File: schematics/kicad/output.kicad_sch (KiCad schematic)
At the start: 33 parts, among them J7 DE15_Socket_HighDensity, K1300 10uF, U1300 HM53461, U1301 HM53461, U1302 HM53461, U1303 HM53461, U1304 HM53461, U1305 HM53461, U1306 HM53461, U1307 HM53461, U1310 BT458, U1311 92.9405Mhz, U1312 10H101, U1313 10H131, U1314 10H350, U1315 LM385BZ-1.2, U1318 74F08

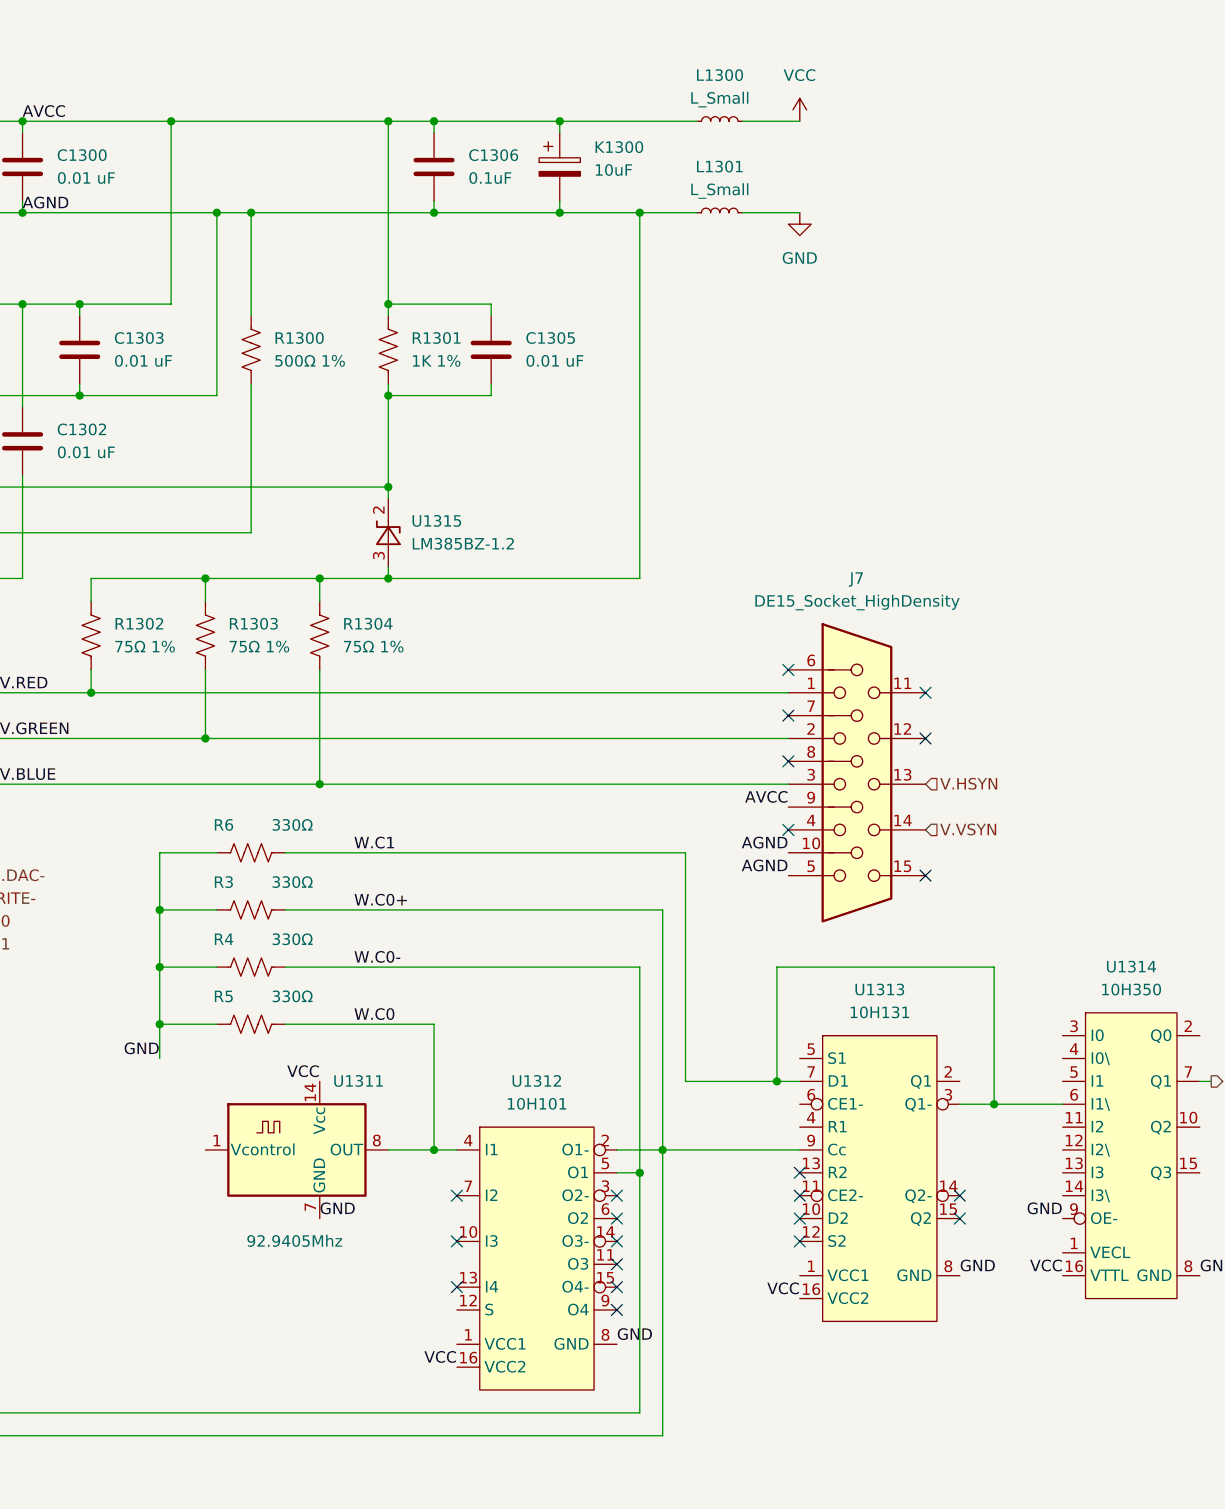
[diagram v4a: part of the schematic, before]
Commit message: Fix layout of the memory chips based on the board Fix the orientation of the P4 connector Connect CS.DAC- based on the board Change the orientation of the ECL resistors to route better Fix the copper islands to match the board, only DAC is on analog island, ECL and crystal are separate. Fix ECL VCC to VCC Confirm VEE not used Add PALs - U1000 missing
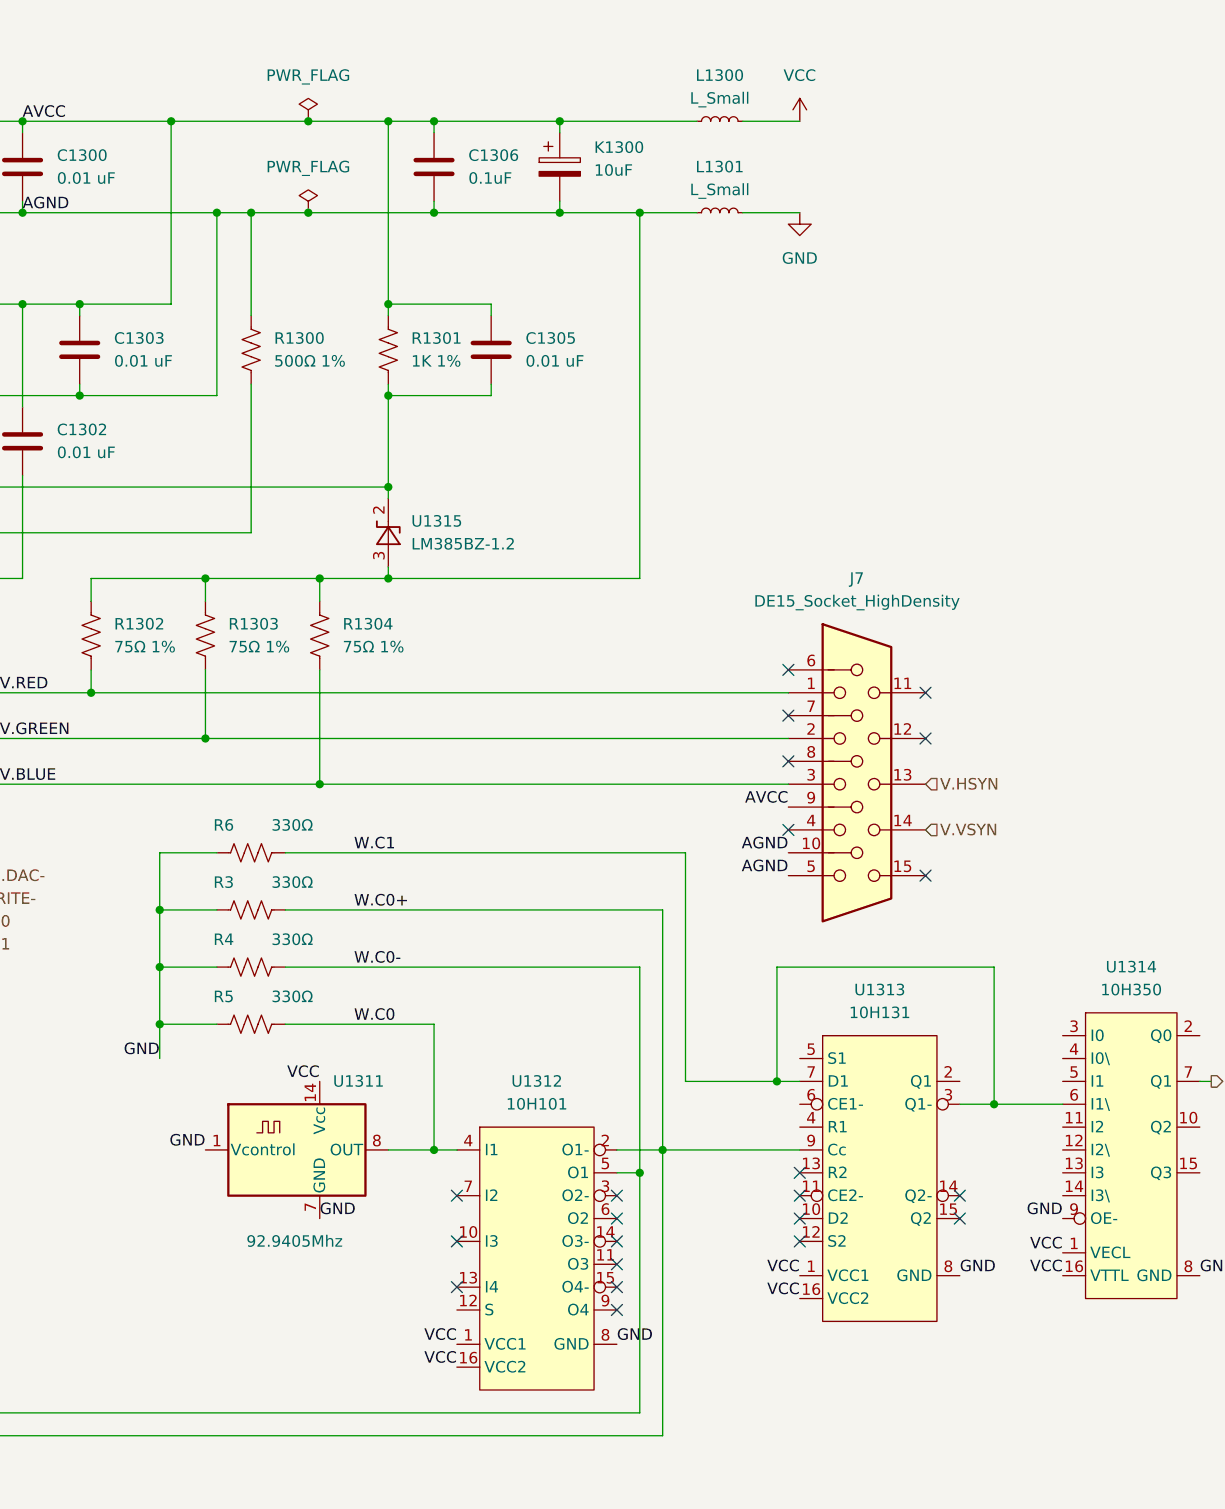
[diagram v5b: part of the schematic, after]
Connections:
- net GND: now also U1311.1 (Vcontrol)
- net VCC: now also U1312.1 (VCC1), U1313.1 (VCC1), U1314.1 (VECL)
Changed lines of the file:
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@@
 	)
 	(junction
+		(at 226.06 24.13)
+		(diameter 0)
+		(color 0 0 0 0)
+	)
+	(junction
 		(at 278.13 130.81)
 		(diameter 0)
@@
 	)
 	(junction
+		(at 226.06 34.29)
+		(diameter 0)
+		(color 0 0 0 0)
+	)
+	(junction
 		(at 55.88 104.14)
 		(diameter 0)
@@
 	(wire
 		(pts
-			(xy 210.82 24.13) (xy 234.95 24.13)
+			(xy 210.82 24.13) (xy 226.06 24.13)
 		)
 		(stroke
@@
 	(wire
 		(pts
+			(xy 226.06 34.29) (xy 240.03 34.29)
+		)
+		(stroke
+			(width 0)
+			(type default)
+		)
+	)
+	(wire
+		(pts
 			(xy 63.5 135.89) (xy 83.82 135.89)
 		)
@@
 	(wire
 		(pts
+			(xy 226.06 24.13) (xy 234.95 24.13)
+		)
+		(stroke
+			(width 0)
+			(type default)
+		)
+	)
+	(wire
+		(pts
 			(xy 214.63 74.93) (xy 227.33 74.93)
 		)
@@
 	(wire
 		(pts
-			(xy 219.71 34.29) (xy 240.03 34.29)
+			(xy 219.71 34.29) (xy 226.06 34.29)
 		)
 		(stroke
@@
 		)
 	)
+	(label "GND"
+		(at 214.63 138.43 180)
+		(effects
+			(font
+				(size 1.27 1.27)
+			)
+			(justify right bottom)
+		)
+	)
 	(label "AGND"
 		(at 279.4 105.41 180)
@@
 		)
 	)
+	(label "VCC"
+		(at 242.57 160.02 180)
+		(effects
+			(font
+				(size 1.27 1.27)
+			)
+			(justify right bottom)
+		)
+	)
 	(label "V.D.D9"
 		(at 130.81 121.92 180)
@@
 		)
 	)
+	(label "VCC"
+		(at 280.67 152.4 180)
+		(effects
+			(font
+				(size 1.27 1.27)
+			)
+			(justify right bottom)
+		)
+	)
 	(label "W.RE-51"
 		(at 76.2 139.7 0)
@@
 		)
 	)
+	(label "VCC"
+		(at 309.88 149.86 180)
+		(effects
+			(font
+				(size 1.27 1.27)
+			)
+			(justify right bottom)
+		)
+	)
 	(label "V.D.D3"
 		(at 163.83 105.41 180)
@@
 	)
 	(symbol
+		(lib_id "power:PWR_FLAG")
+		(at 226.06 34.29 0)
+		(unit 1)
+		(exclude_from_sim no)
+		(in_bom yes)
+		(on_board yes)
+		(dnp no)
+		(fields_autoplaced yes)
+		(property "Reference" "#FLG04"
+			(at 226.06 32.385 0)
+			(effects
+				(font
+					(size 1.27 1.27)
+				)
+				(hide yes)
+			)
+		)
+		(property "Value" "PWR_FLAG"
+			(at 226.06 29.21 0)
+			(effects
+				(font
+					(size 1.27 1.27)
+				)
+			)
+		)
+		(property "Footprint" ""
+			(at 226.06 34.29 0)
+			(effects
+				(font
+					(size 1.27 1.27)
+				)
+				(hide yes)
+			)
+		)
+		(property "Datasheet" "~"
+			(at 226.06 34.29 0)
+			(effects
+				(font
+					(size 1.27 1.27)
+				)
+				(hide yes)
+			)
+		)
+		(property "Description" "Special symbol for telling ERC where power comes from"
+			(at 226.06 34.29 0)
+			(effects
+				(font
+					(size 1.27 1.27)
+				)
+				(hide yes)
+			)
+		)
+		(pin "1"
+		)
+		(instances
+			(project "cg4"
+				(path "/7c2b6a13-c303-4adb-8eed-6e6a9ac5307e/29ede95e-baf3-44af-bd6e-b3be323fd399"
+					(reference "#FLG04")
+					(unit 1)
+				)
+			)
+		)
+	)
+	(symbol
 		(lib_id "power:GND")
 		(at 280.67 34.29 0)
@@
 					(unit 1)
 				)
+			)
+		)
+	)
+	(symbol
+		(lib_id "power:PWR_FLAG")
+		(at 226.06 24.13 0)
+		(unit 1)
+		(exclude_from_sim no)
+		(in_bom yes)
+		(on_board yes)
+		(dnp no)
+		(fields_autoplaced yes)
+		(property "Reference" "#FLG03"
+			(at 226.06 22.225 0)
+			(effects
+				(font
+					(size 1.27 1.27)
+				)
+				(hide yes)
+			)
+		)
+		(property "Value" "PWR_FLAG"
+			(at 226.06 19.05 0)
+			(effects
+				(font
+					(size 1.27 1.27)
+				)
+			)
+		)
+		(property "Footprint" ""
+			(at 226.06 24.13 0)
+			(effects
+				(font
+					(size 1.27 1.27)
+				)
+				(hide yes)
+			)
+		)
+		(property "Datasheet" "~"
+			(at 226.06 24.13 0)
+			(effects
+				(font
+					(size 1.27 1.27)
+				)
+				(hide yes)
+			)
+		)
+		(property "Description" "Special symbol for telling ERC where power comes from"
+			(at 226.06 24.13 0)
+			(effects
+				(font
+					(size 1.27 1.27)
+				)
+				(hide yes)
+			)
+		)
+		(pin "1"
+		)
+		(instances
+			(project "cg4"
+				(path "/7c2b6a13-c303-4adb-8eed-6e6a9ac5307e/29ede95e-baf3-44af-bd6e-b3be323fd399"
+					(reference "#FLG03")
+					(unit 1)
+				)

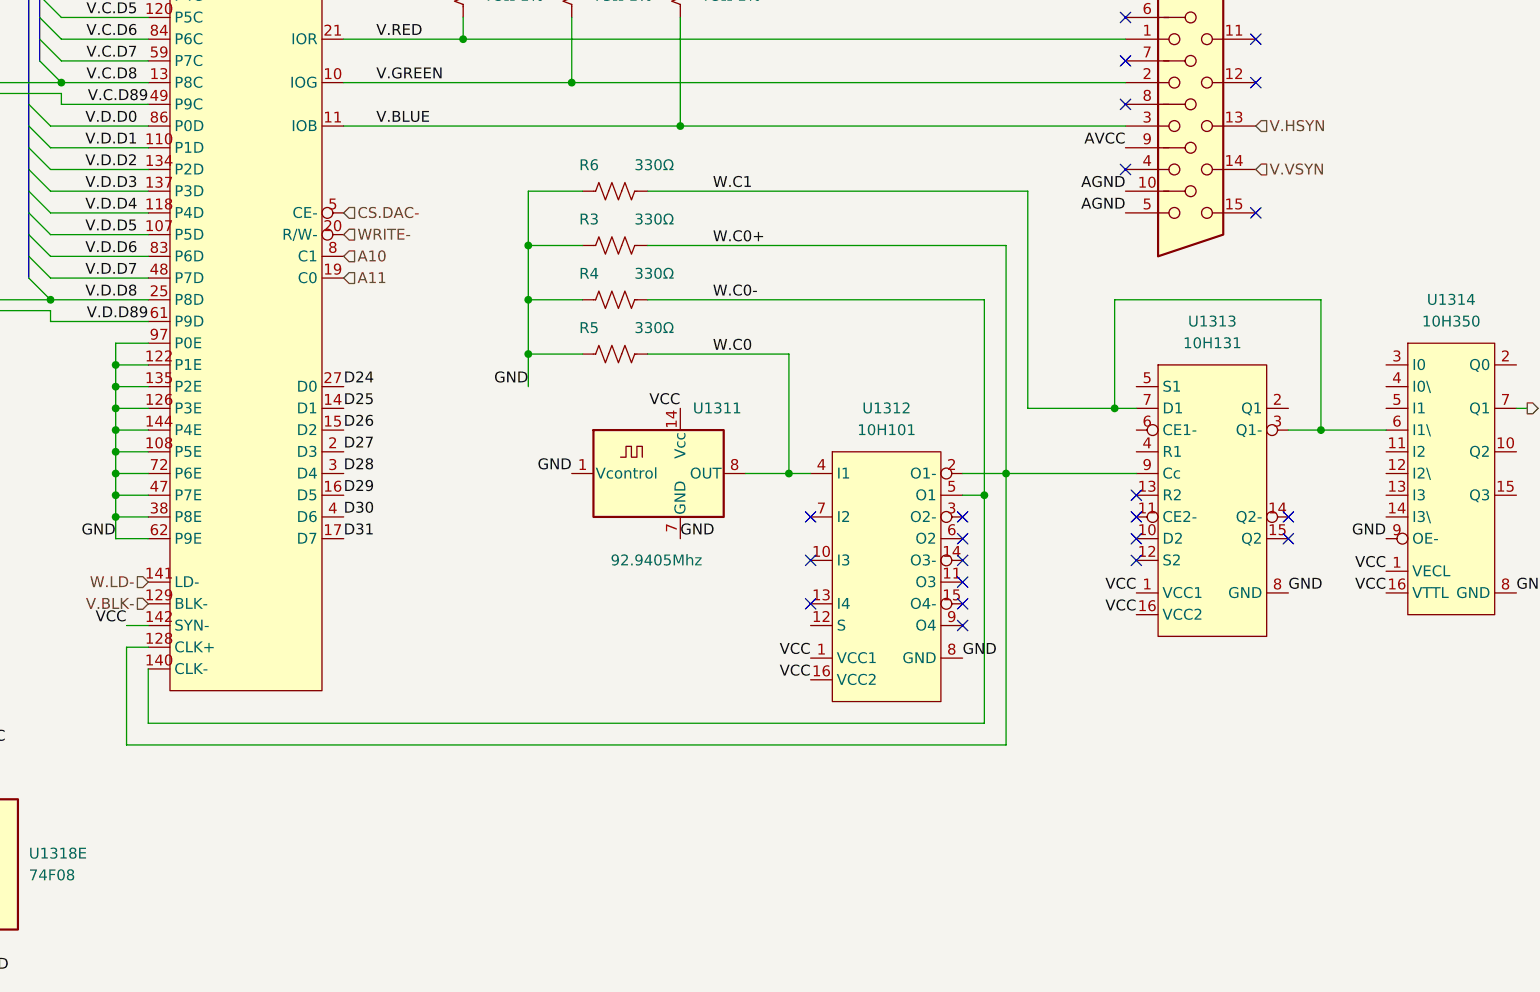
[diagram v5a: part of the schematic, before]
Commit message: More fixes from the physical board tracing. Playing around with layouts: main "cg4" layout is relaxed so it can autoroute. 6layer is the original layout, and the ram_routed is a partial/manually routed version, less relaxed than the main one.
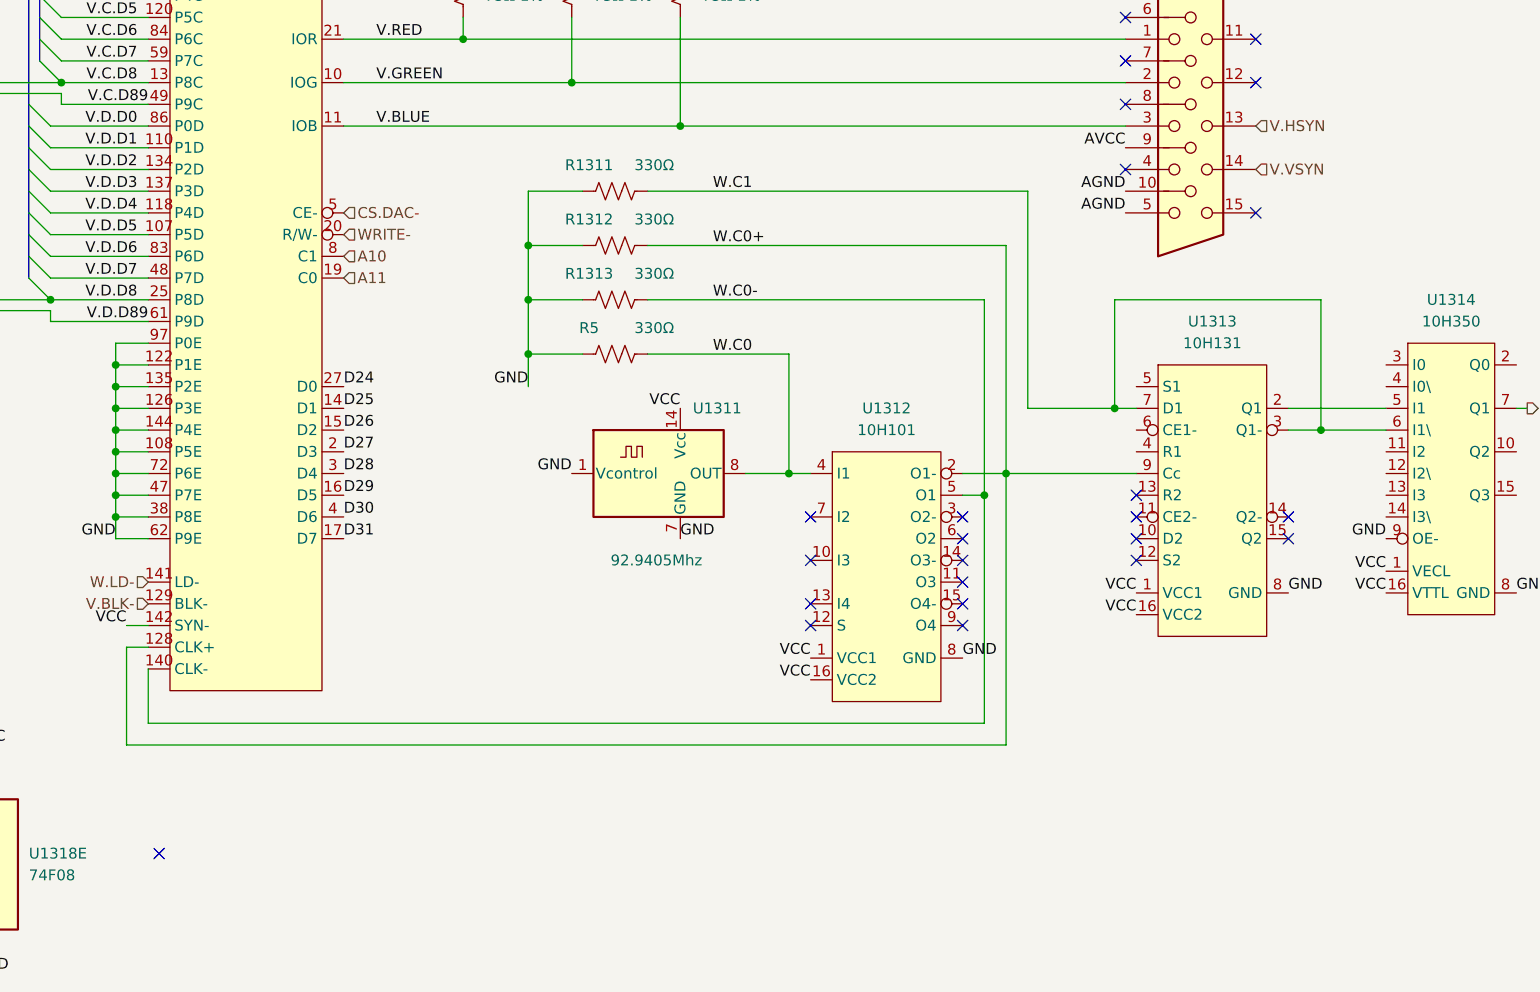
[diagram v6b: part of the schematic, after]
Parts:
- renumbered R6 to R1311, R3 to R1312, R4 to R1313
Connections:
- net at U1314.5 (I1): now also U1313.2 (Q1)
- no-connect marks 23 -> 25
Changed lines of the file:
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@@
 	)
 	(no_connect
+		(at 166.37 182.88)
+	)
+	(no_connect
 		(at 280.67 146.05)
 	)
@@
 	)
 	(no_connect
+		(at 242.57 156.21)
+	)
+	(no_connect
 		(at 260.35 153.67)
 	)
@@
 	(wire
 		(pts
+			(xy 298.45 130.81) (xy 309.88 130.81)
+		)
+		(stroke
+			(width 0)
+			(type default)
+		)
+	)
+	(wire
+		(pts
 			(xy 43.18 118.11) (xy 63.5 118.11)
 		)
@@
 		(on_board yes)
 		(dnp no)
-		(property "Reference" "R4"
+		(property "Reference" "R1313"
 			(at 216.662 115.062 90)
 			(effects
@@
 			(project "cg4"
 				(path "/7c2b6a13-c303-4adb-8eed-6e6a9ac5307e/29ede95e-baf3-44af-bd6e-b3be323fd399"
-					(reference "R4")
+					(reference "R1313")
 					(unit 1)
 				)
@@
 		(on_board yes)
 		(dnp no)
-		(property "Reference" "R6"
+		(property "Reference" "R1311"
 			(at 216.662 102.362 90)
 			(effects
@@
 			(project "cg4"
 				(path "/7c2b6a13-c303-4adb-8eed-6e6a9ac5307e/29ede95e-baf3-44af-bd6e-b3be323fd399"
-					(reference "R6")
+					(reference "R1311")
 					(unit 1)
 				)
@@
 		(on_board yes)
 		(dnp no)
-		(property "Reference" "R3"
+		(property "Reference" "R1312"
 			(at 216.662 108.712 90)
 			(effects
@@
 			(project ""
 				(path "/7c2b6a13-c303-4adb-8eed-6e6a9ac5307e/29ede95e-baf3-44af-bd6e-b3be323fd399"
-					(reference "R3")
+					(reference "R1312")
 					(unit 1)
 				)
